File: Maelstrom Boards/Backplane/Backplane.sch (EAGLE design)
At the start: 4 parts

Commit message: Updated edge connector
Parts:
- removed U$2, U$3, U$4: 5530843-FEMALE, 5530843-6:5530843-FEMALE
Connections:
- removed net SPARE14: U$1.SPARE14, U$2.SPARE14, U$3.SPARE14, U$4.SPARE14
- removed net SPARE15: U$1.SPARE15, U$2.SPARE15, U$3.SPARE15, U$4.SPARE15
- removed net SPARE16: U$1.SPARE16, U$2.SPARE16, U$3.SPARE16, U$4.SPARE16
- new net 12V_ON/OFF: U$1.12V_ON/OFF
- new net 3.3V_ON/OFF: U$1.3.3V_ON/OFF
- new net 5V_ON/OFF: U$1.5V_ON_OFF
- net 3.3V: no longer U$2.3.3V, U$3.3.3V, U$4.3.3V
- net 5V: no longer U$2.5V, U$3.5V, U$4.5V
- net BB_SCL: no longer U$2.BB_SCL, U$3.BB_SCL, U$4.BB_SCL
- net BB_SDA: no longer U$2.BB_SDA, U$3.BB_SDA, U$4.BB_SDA
- net CONV_SCL: no longer U$2.CONV_SCL, U$3.CONV_SCL, U$4.CONV_SCL
- net CONV_SDA: no longer U$2.CONV_SDA, U$3.CONV_SDA, U$4.CONV_SDA
- net ESC_SCL: no longer U$2.ESC_SCL, U$3.ESC_SCL, U$4.ESC_SCL
- net ESC_SDA: no longer U$2.ESC_SDA, U$3.ESC_SDA, U$4.ESC_SDA
- net GND: no longer U$2.GND, U$3.GND, U$4.GND
- net KILL_SWITCH: no longer U$2.KILL_SWITCH, U$3.KILL_SWITCH, U$4.KILL_SWITCH
- net PWM_1: no longer U$2.PWM_1, U$3.PWM_1, U$4.PWM_1
- net PWM_2: no longer U$2.PWM_2, U$3.PWM_2, U$4.PWM_2
- net PWM_3: no longer U$2.PWM_3, U$3.PWM_3, U$4.PWM_3
- net PWM_4: no longer U$2.PWM_4, U$3.PWM_4, U$4.PWM_4
- net PWM_5: no longer U$2.PWM_5, U$3.PWM_5, U$4.PWM_5
- net PWM_6: no longer U$2.PWM_6, U$3.PWM_6, U$4.PWM_6
- net PWM_7: no longer U$2.PWM_7, U$3.PWM_7, U$4.PWM_7
- net PWM_8: no longer U$2.PWM_8, U$3.PWM_8, U$4.PWM_8
- net SPARE1: no longer U$2.SPARE1, U$3.SPARE1, U$4.SPARE1
- net SPARE10: no longer U$2.SPARE10, U$3.SPARE10, U$4.SPARE10
- net SPARE11: no longer U$2.SPARE11, U$3.SPARE11, U$4.SPARE11
- net SPARE12: no longer U$2.SPARE12, U$3.SPARE12, U$4.SPARE12
- net SPARE13: no longer U$2.SPARE13, U$3.SPARE13, U$4.SPARE13
- net SPARE2: no longer U$2.SPARE2, U$3.SPARE2, U$4.SPARE2
- net SPARE3: no longer U$2.SPARE3, U$3.SPARE3, U$4.SPARE3
- net SPARE4: no longer U$2.SPARE4, U$3.SPARE4, U$4.SPARE4
- net SPARE5: no longer U$2.SPARE5, U$3.SPARE5, U$4.SPARE5
- net SPARE6: no longer U$2.SPARE6, U$3.SPARE6, U$4.SPARE6
- net SPARE7: no longer U$2.SPARE7, U$3.SPARE7, U$4.SPARE7
- net SPARE8: no longer U$2.SPARE8, U$3.SPARE8, U$4.SPARE8
- net SPARE9: no longer U$2.SPARE9, U$3.SPARE9, U$4.SPARE9
- net STATUS_SCL: no longer U$2.STATUS_SCL, U$3.STATUS_SCL, U$4.STATUS_SCL
- net STATUS_SDA: no longer U$2.STATUS_SDA, U$3.STATUS_SDA, U$4.STATUS_SDA
- net SWITCH_1: no longer U$2.SWITCH_1, U$3.SWITCH_1, U$4.SWITCH_1
- net SWITCH_2: no longer U$2.SWITCH_2, U$3.SWITCH_2, U$4.SWITCH_2
- net SWITCH_3: no longer U$2.SWITCH_3, U$3.SWITCH_3, U$4.SWITCH_3
- net SWITCH_4: no longer U$2.SWITCH_4, U$3.SWITCH_4, U$4.SWITCH_4
- net SWITCH_5: no longer U$2.SWITCH_5, U$3.SWITCH_5, U$4.SWITCH_5

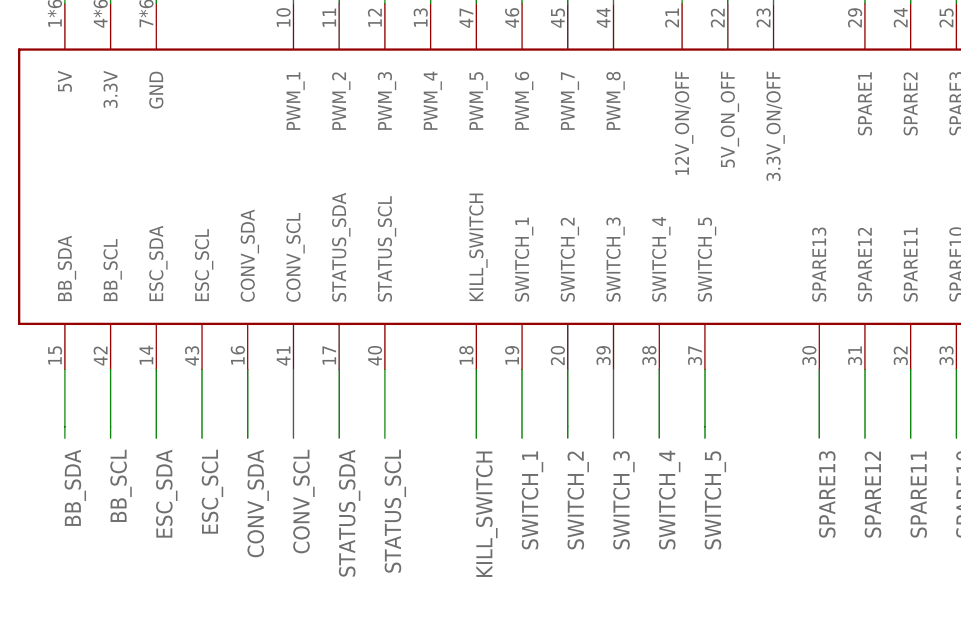
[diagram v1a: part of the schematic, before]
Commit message: Updating edge connector
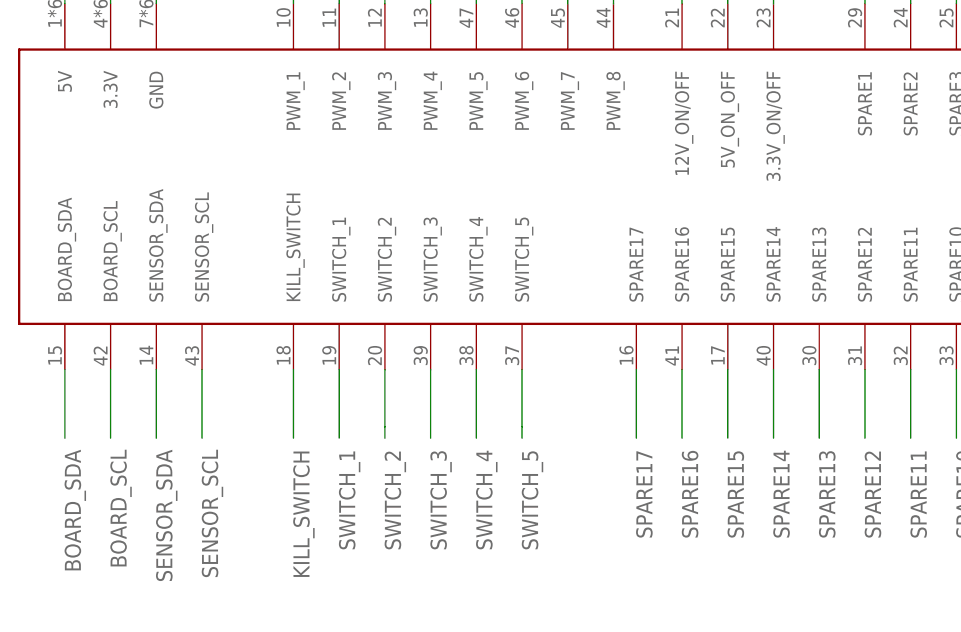
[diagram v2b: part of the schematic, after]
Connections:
- removed net BB_SCL: U$1.BB_SCL
- removed net BB_SDA: U$1.BB_SDA
- removed net CONV_SCL: U$1.CONV_SCL
- removed net CONV_SDA: U$1.CONV_SDA
- removed net ESC_SCL: U$1.ESC_SCL
- removed net ESC_SDA: U$1.ESC_SDA
- removed net STATUS_SCL: U$1.STATUS_SCL
- removed net STATUS_SDA: U$1.STATUS_SDA
- new net BOARD_SCL: U$1.BOARD_SCL
- new net BOARD_SDA: U$1.BOARD_SDA
- new net SENSOR_SCL: U$1.SENSOR_SCL
- new net SENSOR_SDA: U$1.SENSOR_SDA
- new net SPARE14: U$1.SPARE14
- new net SPARE15: U$1.SPARE15
- new net SPARE16: U$1.SPARE16
- new net SPARE17: U$1.SPARE17
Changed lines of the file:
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@@
 </segment>
 </net>
-<net name="BB_SDA" class="0">
-<segment>
-<pinref part="U$1" gate="G$1" pin="BB_SDA"/>
-<wire x1="-15.24" y1="35.56" x2="-15.24" y2="29.21" width="0.1524" layer="91"/>
-<wire x1="-15.24" y1="29.21" x2="-15.24" y2="27.94" width="0.1524" layer="91"/>
-<label x="-15.24" y="26.67" size="1.778" layer="95" rot="R270"/>
-</segment>
-</net>
-<net name="BB_SCL" class="0">
-<segment>
-<pinref part="U$1" gate="G$1" pin="BB_SCL"/>
-<wire x1="-10.16" y1="35.56" x2="-10.16" y2="29.21" width="0.1524" layer="91"/>
-<wire x1="-10.16" y1="29.21" x2="-10.16" y2="27.94" width="0.1524" layer="91"/>
-<label x="-10.16" y="26.67" size="1.778" layer="95" rot="R270"/>
-</segment>
-</net>
-<net name="ESC_SDA" class="0">
-<segment>
-<pinref part="U$1" gate="G$1" pin="ESC_SDA"/>
-<wire x1="-5.08" y1="35.56" x2="-5.08" y2="27.94" width="0.1524" layer="91"/>
-<label x="-5.08" y="26.67" size="1.778" layer="95" rot="R270"/>
-</segment>
-</net>
-<net name="ESC_SCL" class="0">
-<segment>
-<pinref part="U$1" gate="G$1" pin="ESC_SCL"/>
-<wire x1="0" y1="35.56" x2="0" y2="27.94" width="0.1524" layer="91"/>
-<label x="0" y="26.67" size="1.778" layer="95" rot="R270"/>
-</segment>
-</net>
-<net name="CONV_SDA" class="0">
-<segment>
-<pinref part="U$1" gate="G$1" pin="CONV_SDA"/>
-<wire x1="5.08" y1="35.56" x2="5.08" y2="27.94" width="0.1524" layer="91"/>
-<label x="5.08" y="26.67" size="1.778" layer="95" rot="R270"/>
-</segment>
-</net>
-<net name="CONV_SCL" class="0">
-<segment>
-<pinref part="U$1" gate="G$1" pin="CONV_SCL"/>
+<net name="SWITCH_1" class="0">
+<segment>
+<pinref part="U$1" gate="G$1" pin="SWITCH_1"/>
+<wire x1="15.24" y1="35.56" x2="15.24" y2="27.94" width="0.1524" layer="91"/>
+<label x="15.24" y="26.67" size="1.778" layer="95" rot="R270"/>
+</segment>
+</net>
+<net name="SWITCH_2" class="0">
+<segment>
+<pinref part="U$1" gate="G$1" pin="SWITCH_2"/>
+<wire x1="20.32" y1="35.56" x2="20.32" y2="29.21" width="0.1524" layer="91"/>
+<wire x1="20.32" y1="29.21" x2="20.32" y2="27.94" width="0.1524" layer="91"/>
+<label x="20.32" y="26.67" size="1.778" layer="95" rot="R270"/>
+</segment>
+</net>
+<net name="SWITCH_3" class="0">
+<segment>
+<pinref part="U$1" gate="G$1" pin="SWITCH_3"/>
+<wire x1="25.4" y1="35.56" x2="25.4" y2="27.94" width="0.1524" layer="91"/>
+<label x="25.4" y="26.67" size="1.778" layer="95" rot="R270"/>
+</segment>
+</net>
+<net name="SWITCH_4" class="0">
+<segment>
+<pinref part="U$1" gate="G$1" pin="SWITCH_4"/>
+<wire x1="30.48" y1="35.56" x2="30.48" y2="27.94" width="0.1524" layer="91"/>
+<label x="30.48" y="26.67" size="1.778" layer="95" rot="R270"/>
+</segment>
+</net>
+<net name="KILL_SWITCH" class="0">
+<segment>
+<pinref part="U$1" gate="G$1" pin="KILL_SWITCH"/>
 <wire x1="10.16" y1="35.56" x2="10.16" y2="27.94" width="0.1524" layer="91"/>
 <label x="10.16" y="26.67" size="1.778" layer="95" rot="R270"/>
 </segment>
 </net>
-<net name="STATUS_SDA" class="0">
-<segment>
-<pinref part="U$1" gate="G$1" pin="STATUS_SDA"/>
-<wire x1="15.24" y1="35.56" x2="15.24" y2="27.94" width="0.1524" layer="91"/>
-<label x="15.24" y="26.67" size="1.778" layer="95" rot="R270"/>
-</segment>
-</net>
-<net name="STATUS_SCL" class="0">
-<segment>
-<pinref part="U$1" gate="G$1" pin="STATUS_SCL"/>
-<wire x1="20.32" y1="35.56" x2="20.32" y2="27.94" width="0.1524" layer="91"/>
-<label x="20.32" y="26.67" size="1.778" layer="95" rot="R270"/>
-</segment>
-</net>
-<net name="SWITCH_1" class="0">
-<segment>
-<pinref part="U$1" gate="G$1" pin="SWITCH_1"/>
-<wire x1="35.56" y1="35.56" x2="35.56" y2="27.94" width="0.1524" layer="91"/>
+<net name="SWITCH_5" class="0">
+<segment>
+<pinref part="U$1" gate="G$1" pin="SWITCH_5"/>
+<wire x1="35.56" y1="35.56" x2="35.56" y2="29.21" width="0.1524" layer="91"/>
+<wire x1="35.56" y1="29.21" x2="35.56" y2="27.94" width="0.1524" layer="91"/>
 <label x="35.56" y="26.67" size="1.778" layer="95" rot="R270"/>
-</segment>
-</net>
-<net name="SWITCH_2" class="0">
-<segment>
-<pinref part="U$1" gate="G$1" pin="SWITCH_2"/>
-<wire x1="40.64" y1="35.56" x2="40.64" y2="29.21" width="0.1524" layer="91"/>
-<wire x1="40.64" y1="29.21" x2="40.64" y2="27.94" width="0.1524" layer="91"/>
-<label x="40.64" y="26.67" size="1.778" layer="95" rot="R270"/>
-</segment>
-</net>
-<net name="SWITCH_3" class="0">
-<segment>
-<pinref part="U$1" gate="G$1" pin="SWITCH_3"/>
-<wire x1="45.72" y1="35.56" x2="45.72" y2="27.94" width="0.1524" layer="91"/>
-<label x="45.72" y="26.67" size="1.778" layer="95" rot="R270"/>
-</segment>
-</net>
-<net name="SWITCH_4" class="0">
-<segment>
-<pinref part="U$1" gate="G$1" pin="SWITCH_4"/>
-<wire x1="50.8" y1="35.56" x2="50.8" y2="27.94" width="0.1524" layer="91"/>
-<label x="50.8" y="26.67" size="1.778" layer="95" rot="R270"/>
-</segment>
-</net>
-<net name="KILL_SWITCH" class="0">
-<segment>
-<pinref part="U$1" gate="G$1" pin="KILL_SWITCH"/>
-<wire x1="30.48" y1="35.56" x2="30.48" y2="27.94" width="0.1524" layer="91"/>
-<label x="30.48" y="26.67" size="1.778" layer="95" rot="R270"/>
-</segment>
-</net>
-<net name="SWITCH_5" class="0">
-<segment>
-<pinref part="U$1" gate="G$1" pin="SWITCH_5"/>
-<wire x1="55.88" y1="35.56" x2="55.88" y2="29.21" width="0.1524" layer="91"/>
-<wire x1="55.88" y1="29.21" x2="55.88" y2="27.94" width="0.1524" layer="91"/>
-<label x="55.88" y="26.67" size="1.778" layer="95" rot="R270"/>
 </segment>
 </net>
@@
 </segment>
 </net>
+<net name="SENSOR_SCL" class="0">
+<segment>
+<pinref part="U$1" gate="G$1" pin="SENSOR_SCL"/>
+<wire x1="0" y1="35.56" x2="0" y2="27.94" width="0.1524" layer="91"/>
+<label x="0" y="26.67" size="1.778" layer="95" rot="R270"/>
+</segment>
+</net>
+<net name="SENSOR_SDA" class="0">
+<segment>
+<pinref part="U$1" gate="G$1" pin="SENSOR_SDA"/>
+<wire x1="-5.08" y1="35.56" x2="-5.08" y2="27.94" width="0.1524" layer="91"/>
+<label x="-5.08" y="26.67" size="1.778" layer="95" rot="R270"/>
+</segment>
+</net>
+<net name="BOARD_SCL" class="0">
+<segment>
+<pinref part="U$1" gate="G$1" pin="BOARD_SCL"/>
+<wire x1="-10.16" y1="35.56" x2="-10.16" y2="27.94" width="0.1524" layer="91"/>
+<label x="-10.16" y="26.67" size="1.778" layer="95" rot="R270"/>
+</segment>
+</net>
+<net name="BOARD_SDA" class="0">
+<segment>
+<pinref part="U$1" gate="G$1" pin="BOARD_SDA"/>
+<wire x1="-15.24" y1="35.56" x2="-15.24" y2="27.94" width="0.1524" layer="91"/>
+<label x="-15.24" y="26.67" size="1.778" layer="95" rot="R270"/>
+</segment>
+</net>
+<net name="SPARE14" class="0">
+<segment>
+<pinref part="U$1" gate="G$1" pin="SPARE14"/>
+<wire x1="63.5" y1="35.56" x2="63.5" y2="27.94" width="0.1524" layer="91"/>
+<label x="63.5" y="26.67" size="1.778" layer="95" rot="R270"/>
+</segment>
+</net>
+<net name="SPARE15" class="0">
+<segment>
+<pinref part="U$1" gate="G$1" pin="SPARE15"/>
+<wire x1="58.42" y1="35.56" x2="58.42" y2="27.94" width="0.1524" layer="91"/>
+<label x="58.42" y="26.67" size="1.778" layer="95" rot="R270"/>
+</segment>
+</net>
+<net name="SPARE16" class="0">
+<segment>
+<pinref part="U$1" gate="G$1" pin="SPARE16"/>
+<wire x1="53.34" y1="35.56" x2="53.34" y2="27.94" width="0.1524" layer="91"/>
+<label x="53.34" y="26.67" size="1.778" layer="95" rot="R270"/>
+</segment>
+</net>
+<net name="SPARE17" class="0">
+<segment>
+<pinref part="U$1" gate="G$1" pin="SPARE17"/>
+<wire x1="48.26" y1="35.56" x2="48.26" y2="27.94" width="0.1524" layer="91"/>
+<label x="48.26" y="26.67" size="1.778" layer="95" rot="R270"/>
+</segment>
+</net>

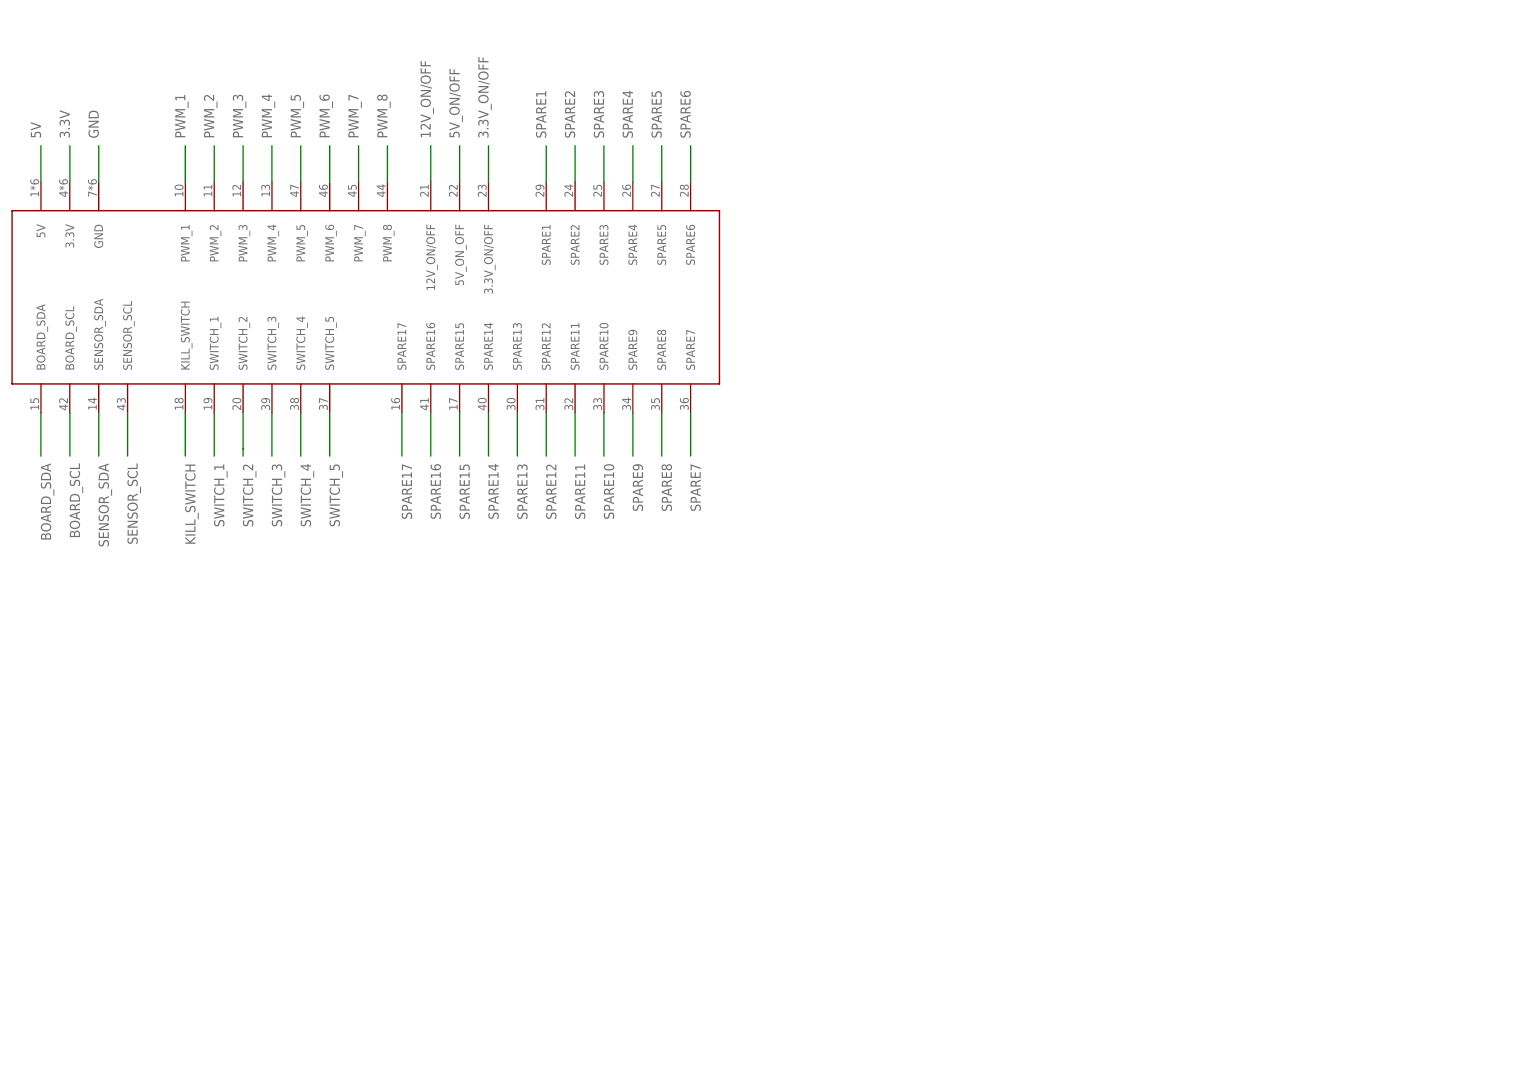
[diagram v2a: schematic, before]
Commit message: added portsto backplane
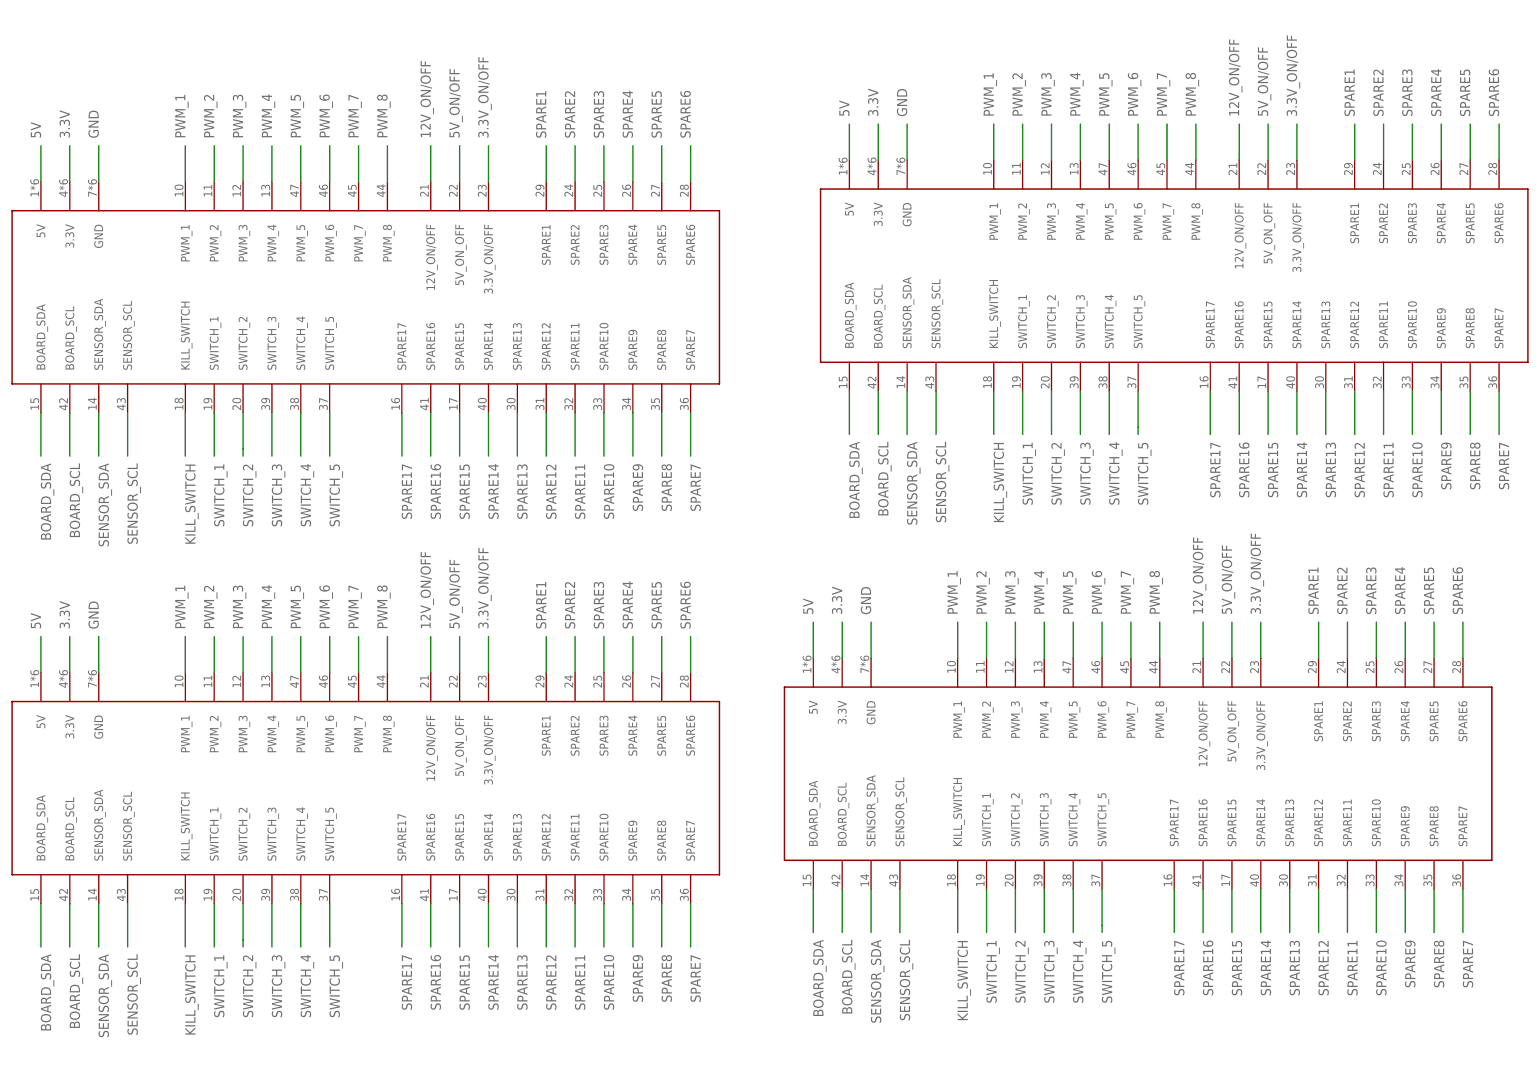
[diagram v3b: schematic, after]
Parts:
- added U$2, U$3, U$4: 5530843-FEMALE, 5530843-6:5530843-FEMALE
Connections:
- net 12V_ON/OFF: now also U$2.12V_ON/OFF, U$3.12V_ON/OFF, U$4.12V_ON/OFF
- net 3.3V: now also U$2.3.3V, U$3.3.3V, U$4.3.3V
- net 3.3V_ON/OFF: now also U$2.3.3V_ON/OFF, U$3.3.3V_ON/OFF, U$4.3.3V_ON/OFF
- net 5V: now also U$2.5V, U$3.5V, U$4.5V
- net 5V_ON/OFF: now also U$2.5V_ON_OFF, U$3.5V_ON_OFF, U$4.5V_ON_OFF
- net BOARD_SCL: now also U$2.BOARD_SCL, U$3.BOARD_SCL, U$4.BOARD_SCL
- net BOARD_SDA: now also U$2.BOARD_SDA, U$3.BOARD_SDA, U$4.BOARD_SDA
- net GND: now also U$2.GND, U$3.GND, U$4.GND
- net KILL_SWITCH: now also U$2.KILL_SWITCH, U$3.KILL_SWITCH, U$4.KILL_SWITCH
- net PWM_1: now also U$2.PWM_1, U$3.PWM_1, U$4.PWM_1
- net PWM_2: now also U$2.PWM_2, U$3.PWM_2, U$4.PWM_2
- net PWM_3: now also U$2.PWM_3, U$3.PWM_3, U$4.PWM_3
- net PWM_4: now also U$2.PWM_4, U$3.PWM_4, U$4.PWM_4
- net PWM_5: now also U$2.PWM_5, U$3.PWM_5, U$4.PWM_5
- net PWM_6: now also U$2.PWM_6, U$3.PWM_6, U$4.PWM_6
- net PWM_7: now also U$2.PWM_7, U$3.PWM_7, U$4.PWM_7
- net PWM_8: now also U$2.PWM_8, U$3.PWM_8, U$4.PWM_8
- net SENSOR_SCL: now also U$2.SENSOR_SCL, U$3.SENSOR_SCL, U$4.SENSOR_SCL
- net SENSOR_SDA: now also U$2.SENSOR_SDA, U$3.SENSOR_SDA, U$4.SENSOR_SDA
- net SPARE1: now also U$2.SPARE1, U$3.SPARE1, U$4.SPARE1
- net SPARE10: now also U$2.SPARE10, U$3.SPARE10, U$4.SPARE10
- net SPARE11: now also U$2.SPARE11, U$3.SPARE11, U$4.SPARE11
- net SPARE12: now also U$2.SPARE12, U$3.SPARE12, U$4.SPARE12
- net SPARE13: now also U$2.SPARE13, U$3.SPARE13, U$4.SPARE13
- net SPARE14: now also U$2.SPARE14, U$3.SPARE14, U$4.SPARE14
- net SPARE15: now also U$2.SPARE15, U$3.SPARE15, U$4.SPARE15
- net SPARE16: now also U$2.SPARE16, U$3.SPARE16, U$4.SPARE16
- net SPARE17: now also U$2.SPARE17, U$3.SPARE17, U$4.SPARE17
- net SPARE2: now also U$2.SPARE2, U$3.SPARE2, U$4.SPARE2
- net SPARE3: now also U$2.SPARE3, U$3.SPARE3, U$4.SPARE3
- net SPARE4: now also U$2.SPARE4, U$3.SPARE4, U$4.SPARE4
- net SPARE5: now also U$2.SPARE5, U$3.SPARE5, U$4.SPARE5
- net SPARE6: now also U$2.SPARE6, U$3.SPARE6, U$4.SPARE6
- net SPARE7: now also U$2.SPARE7, U$3.SPARE7, U$4.SPARE7
- net SPARE8: now also U$2.SPARE8, U$3.SPARE8, U$4.SPARE8
- net SPARE9: now also U$2.SPARE9, U$3.SPARE9, U$4.SPARE9
- net SWITCH_1: now also U$2.SWITCH_1, U$3.SWITCH_1, U$4.SWITCH_1
- net SWITCH_2: now also U$2.SWITCH_2, U$3.SWITCH_2, U$4.SWITCH_2
- net SWITCH_3: now also U$2.SWITCH_3, U$3.SWITCH_3, U$4.SWITCH_3
- net SWITCH_4: now also U$2.SWITCH_4, U$3.SWITCH_4, U$4.SWITCH_4
- net SWITCH_5: now also U$2.SWITCH_5, U$3.SWITCH_5, U$4.SWITCH_5
